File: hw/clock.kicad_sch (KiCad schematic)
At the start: 33 parts, among them J1 USB4105-GF-A, SW1 SW_Push, SW2 SW_Push, U1 LPC812M101JDH20, U2 INTERFACE-FT230XS-R_SSOP16_, U3 SN74HC595DR, U4 SN74HC595DR, U5 SN74HC595DR, U6 SN74HC595DR, U7 SN74HC595DR, U8 SN74HC595DR, U9 MCP7940MT-I_SN, Y1 30MHz, Y2 32.768KHz

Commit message: Displays
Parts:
- added R11: 10k, Resistor_SMD:R_0805_2012Metric, symbol Device:R_US
- added U10, U11, U12: HDSP-5321 Common Anode, symbol Display_Character:HDSP-5321
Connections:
- net 0_A is gone; now on net 1_A: U3.15 (QA)
- net 0_B is gone; now on net 1_B: U3.1 (QB)
- net 0_C is gone; now on net 1_C: U3.2 (QC)
- net 0_D is gone; now on net 1_D: U3.3 (QD)
- net 0_E is gone; now on net 1_E: U3.4 (QE)
- net 0_F is gone; now on net 1_F: U3.5 (QF)
- net 0_G is gone; now on net 1_G: U3.6 (QG)
- net 0_H is gone; now on net 1_H: U3.9 (QH)
- net +3V3: now also R1.2, R10.2, R11.2; no longer SW1.1, SW2.1, U2.11 (RESET)
- net 1_A: now also U10.16 (A1); no longer U4.15 (QA)
- net 1_B: now also U10.15 (B1); no longer U4.1 (QB)
- net 1_C: now also U10.3 (C1); no longer U4.2 (QC)
- net 1_D: now also U10.2 (D1); no longer U4.3 (QD)
- net 1_E: now also U10.1 (E1); no longer U4.4 (QE)
- net 1_F: now also U10.18 (F1); no longer U4.5 (QF)
- net 1_G: now also U10.17 (G1); no longer U4.6 (QG)
- net 1_H: now also U10.4 (DP1); no longer U4.9 (QH)
- net 2_A: now also U4.15 (QA), U10.11 (A2); no longer U5.15 (QA)
- net 2_B: now also U4.1 (QB), U10.10 (B2); no longer U5.1 (QB)
- net 2_C: now also U4.2 (QC), U10.8 (C2); no longer U5.2 (QC)
- net 2_D: now also U4.3 (QD), U10.6 (D2); no longer U5.3 (QD)
- net 2_E: now also U4.4 (QE), U10.5 (E2); no longer U5.4 (QE)
- net 2_F: now also U4.5 (QF), U10.12 (F2); no longer U5.5 (QF)
- net 2_G: now also U4.6 (QG), U10.7 (G2); no longer U5.6 (QG)
- net 2_H: now also U4.9 (QH), U10.9 (DP2); no longer U5.9 (QH)
- net 3_A: now also U5.15 (QA), U11.16 (A1); no longer U6.15 (QA)
- net 3_B: now also U5.1 (QB), U11.15 (B1); no longer U6.1 (QB)
- net 3_C: now also U5.2 (QC), U11.3 (C1); no longer U6.2 (QC)
- net 3_D: now also U5.3 (QD), U11.2 (D1); no longer U6.3 (QD)
- net 3_E: now also U5.4 (QE), U11.1 (E1); no longer U6.4 (QE)
- net 3_F: now also U5.5 (QF), U11.18 (F1); no longer U6.5 (QF)
- net 3_G: now also U5.6 (QG), U11.17 (G1); no longer U6.6 (QG)
- net 3_H: now also U5.9 (QH), U11.4 (DP1); no longer U6.9 (QH)
- net 4_A: now also U6.15 (QA), U11.11 (A2); no longer U7.15 (QA)
- net 4_B: now also U6.1 (QB), U11.10 (B2); no longer U7.1 (QB)
- net 4_C: now also U6.2 (QC), U11.8 (C2); no longer U7.2 (QC)
- net 4_D: now also U6.3 (QD), U11.6 (D2); no longer U7.3 (QD)
- net 4_E: now also U6.4 (QE), U11.5 (E2); no longer U7.4 (QE)
- net 4_F: now also U6.5 (QF), U11.12 (F2); no longer U7.5 (QF)
- net 4_G: now also U6.6 (QG), U11.7 (G2); no longer U7.6 (QG)
- net 4_H: now also U6.9 (QH), U11.9 (DP2); no longer U7.9 (QH)
- net 5_A: now also U7.15 (QA), U12.16 (A1); no longer U8.15 (QA)
- net 5_B: now also U7.1 (QB), U12.15 (B1); no longer U8.1 (QB)
- net 5_C: now also U7.2 (QC), U12.3 (C1); no longer U8.2 (QC)
- net 5_D: now also U7.3 (QD), U12.2 (D1); no longer U8.3 (QD)
- net 5_E: now also U7.4 (QE), U12.1 (E1); no longer U8.4 (QE)
- net 5_F: now also U7.5 (QF), U12.18 (F1); no longer U8.5 (QF)
- net 5_G: now also U7.6 (QG), U12.17 (G1); no longer U8.6 (QG)
- net 5_H: now also U7.9 (QH), U12.4 (DP1); no longer U8.9 (QH)
- net GND: now also SW1.2, SW2.2, U3.13 (~{OE}), U4.13 (~{OE}), U5.13 (~{OE}), U6.13 (~{OE}), U7.13 (~{OE}), U8.13 (~{OE}); no longer R1.1, R10.1
- net SHIFT_CLR: now also R10.1, SW2.1; no longer R10.2, SW2.2
- net SHIFT_SER_1: now also U3.14 (SER); no longer U4.14 (SER)
- net SHIFT_SER_2: now also U4.14 (SER); no longer U5.14 (SER)
- net SHIFT_SER_3: now also U5.14 (SER); no longer U6.14 (SER)
- net SHIFT_SER_4: now also U6.14 (SER); no longer U7.14 (SER)
- net SHIFT_SER_5: now also U7.14 (SER); no longer U8.14 (SER)
- removed net SHIFT_OUT: R1.2, SW1.2, U1.4 (PIO0_5), U3.13 (~{OE}), U4.13 (~{OE}), U5.13 (~{OE}), U6.13 (~{OE}), U7.13 (~{OE}), U8.13 (~{OE})
- net SHIFT_SER_0 renamed SHIFT_SER_6
- net SHIFT_SER_6: now also U8.14 (SER); no longer U3.14 (SER)
- new net 6_A: U12.11 (A2), U8.15 (QA)
- new net 6_B: U12.10 (B2), U8.1 (QB)
- new net 6_C: U12.8 (C2), U8.2 (QC)
- new net 6_D: U12.6 (D2), U8.3 (QD)
- new net 6_E: U12.5 (E2), U8.4 (QE)
- new net 6_F: U12.12 (F2), U8.5 (QF)
- new net 6_G: U12.7 (G2), U8.6 (QG)
- new net 6_H: U12.9 (DP2), U8.9 (QH)
- new net DISPLAY_PWR: R11.1, U10.13 (Vcc2), U10.14 (Vcc1), U11.13 (Vcc2), U11.14 (Vcc1), U12.13 (Vcc2), U12.14 (Vcc1)
- new net RESET: R1.1, SW1.1, U1.4 (PIO0_5), U2.11 (RESET)
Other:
- note added: "Displays"
- note added: "ISP"
- note added: "Registers 1 and 2"
- note added: "Registers 3 and 4"
- note added: "Registers 5 and 6"
- moved on the sheet: C1, C2, C3, C4, D1, D2, D3, J1, R2, R3, R4, R5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

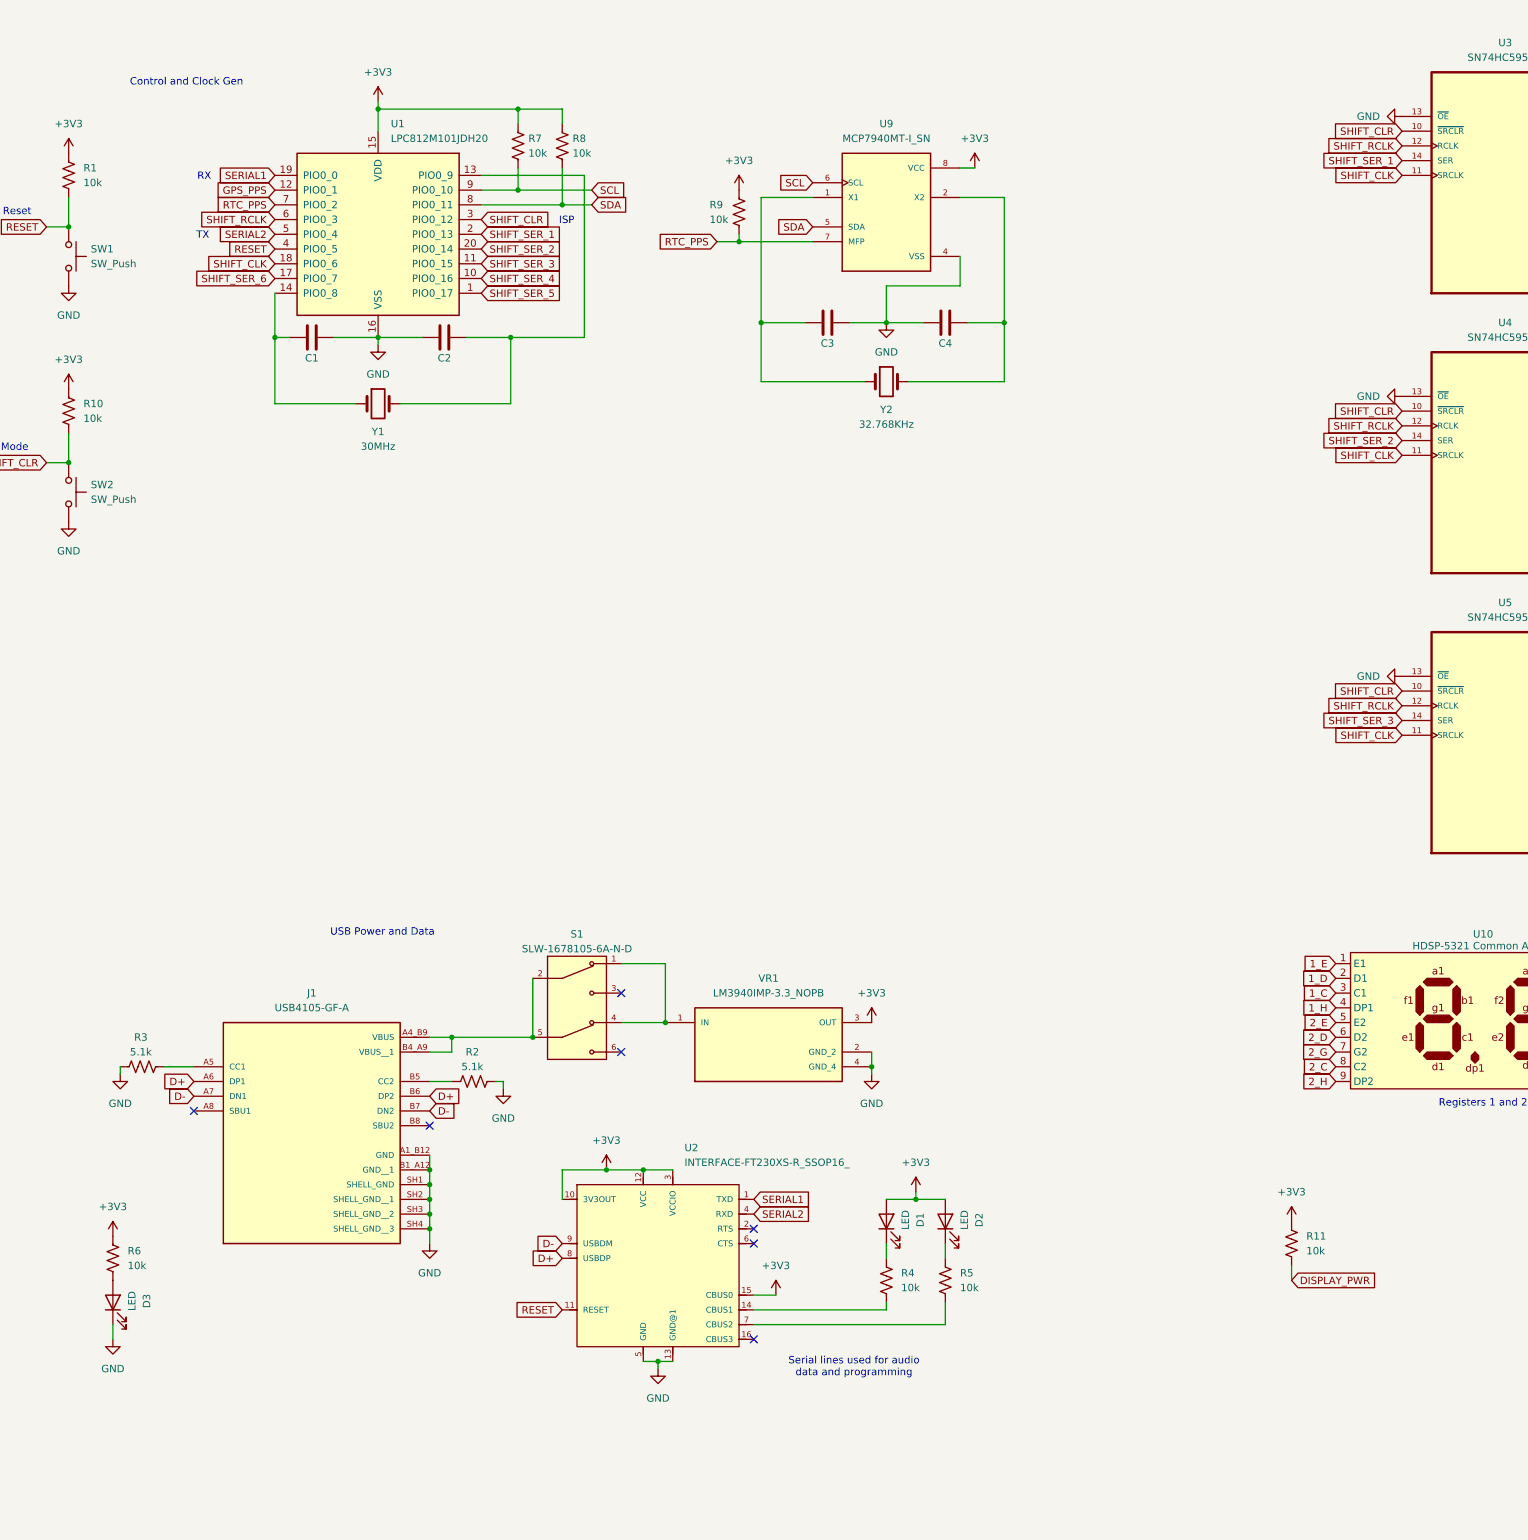
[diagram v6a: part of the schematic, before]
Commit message: Variable brightness, temperature sense
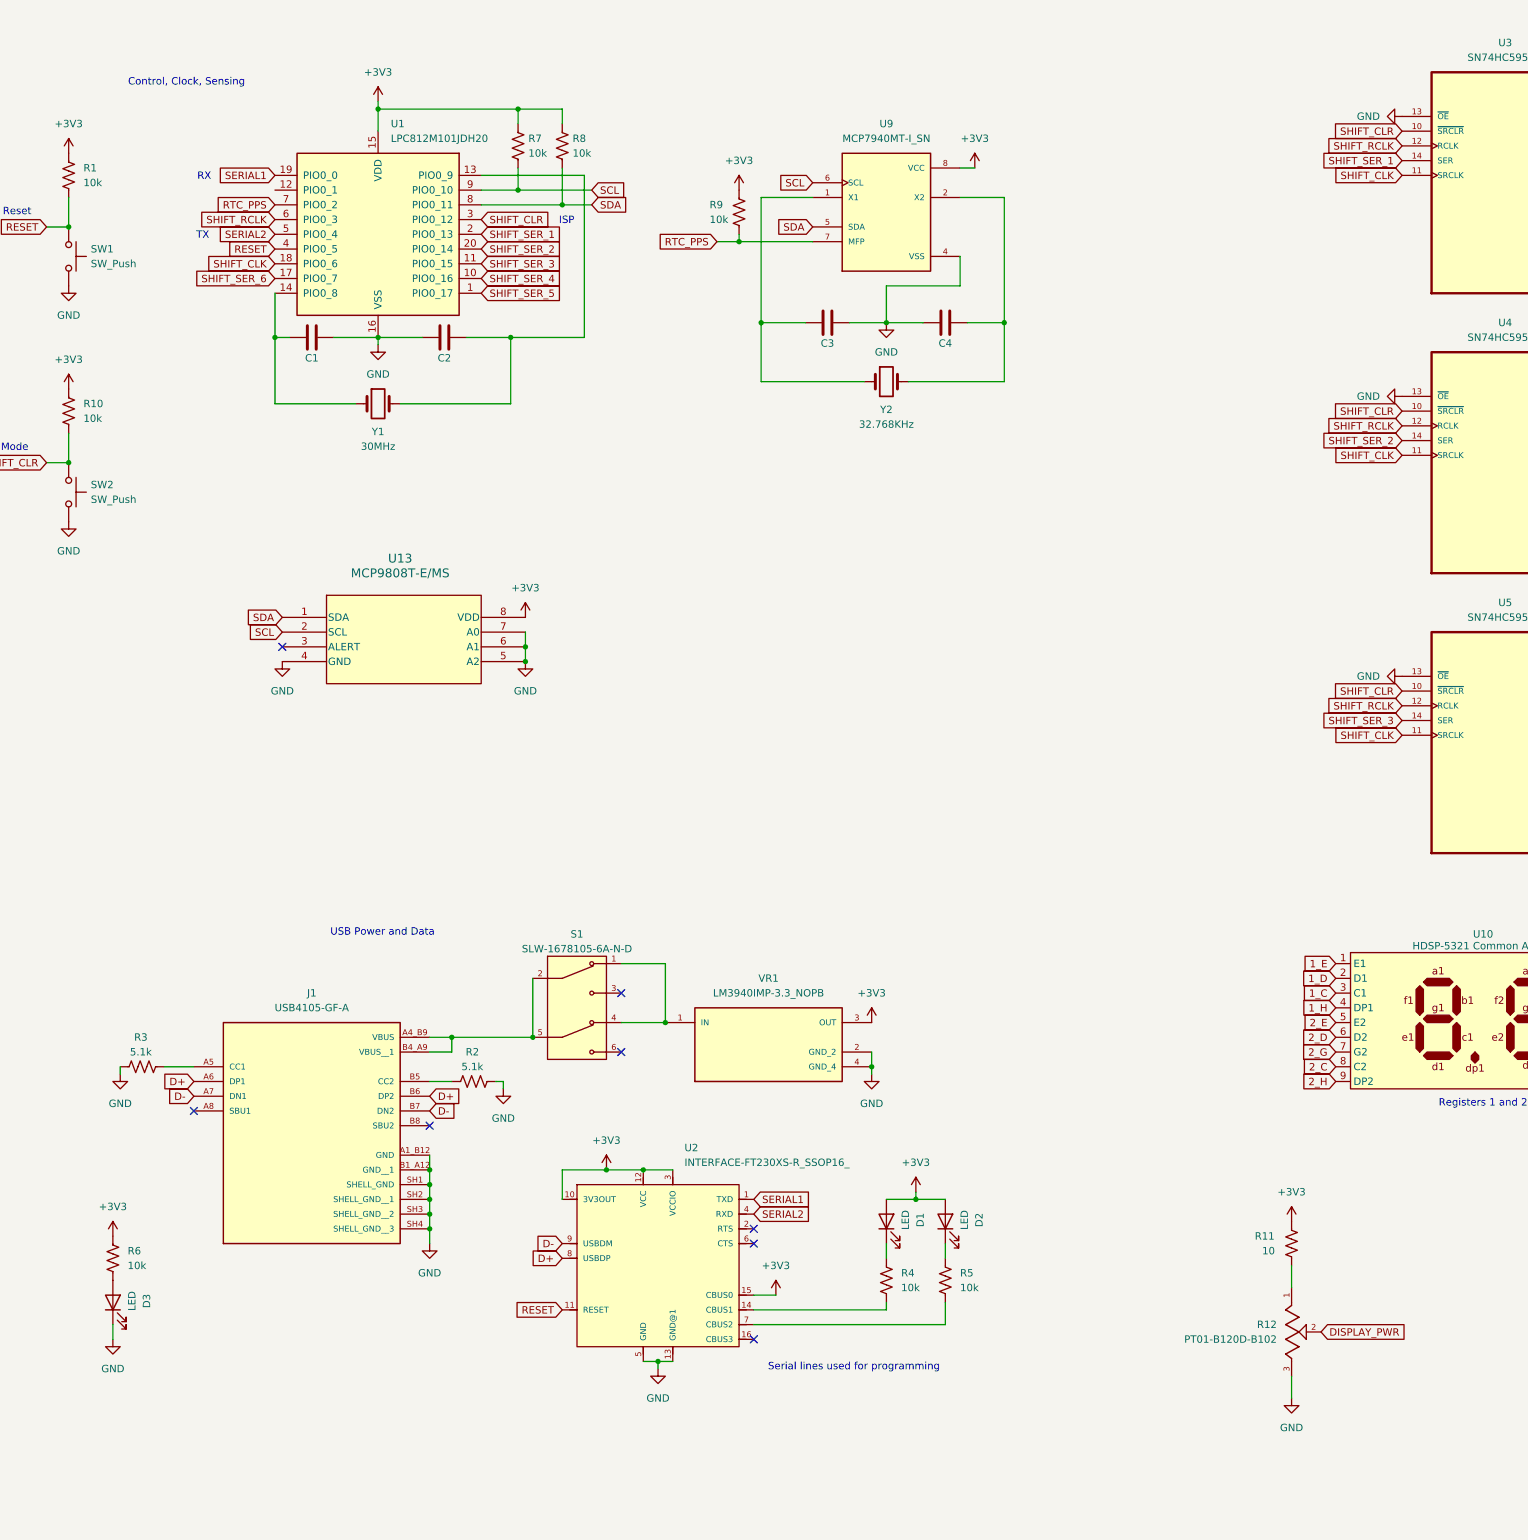
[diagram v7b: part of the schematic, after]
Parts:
- added R12: PT01-B120D-B102, PT01-B120D-B102:TRIM_PT01-B120D-B102, symbol PT01-B120D-B102:PT01-B120D-B102
- added U13: MCP9808T-E/MS, MSOP8_MC_MCH, symbol MCP9808T_E_MS:MCP9808T-E_MS
- R11: value 10k -> 10
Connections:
- net +3V3: now also U13.8 (VDD)
- net DISPLAY_PWR: now also R12.2; no longer R11.1
- net GND: now also R12.3, U13.4 (GND), U13.5 (A2), U13.6 (A1), U13.7 (A0)
- net SCL: now also U13.2 (SCL)
- net SDA: now also U13.1 (SDA)
- net GPS_PPS: no longer names the net of U1.12 (PIO0_1)
- new net: R11.1, R12.1
- no-connect marks 13 -> 14
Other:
- note added: "Control, Clock, Sensing"
- note added: "Serial lines used for programming"
- note removed: "Control and Clock Gen"
- note removed: "Serial lines used for audio data and programming"
